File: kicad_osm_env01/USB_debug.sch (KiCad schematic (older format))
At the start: 22 parts, among them Q2 S8050, Q3 S8050, U13 CP2102N-A01-GQFN24

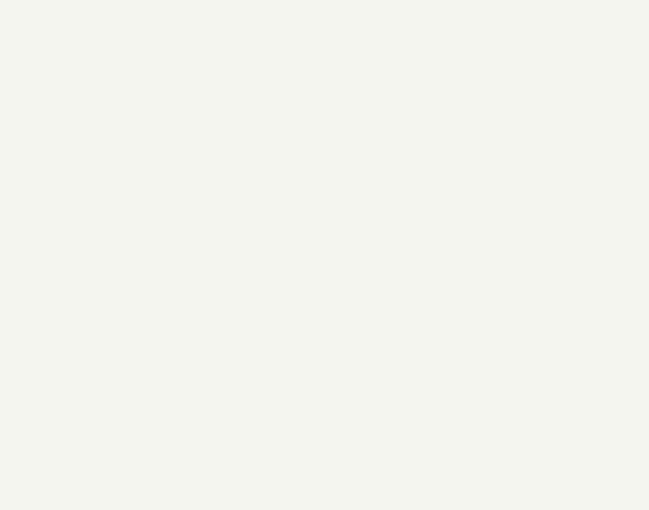
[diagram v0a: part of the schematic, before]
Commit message: pushed latest schematics got started with micro into schematic
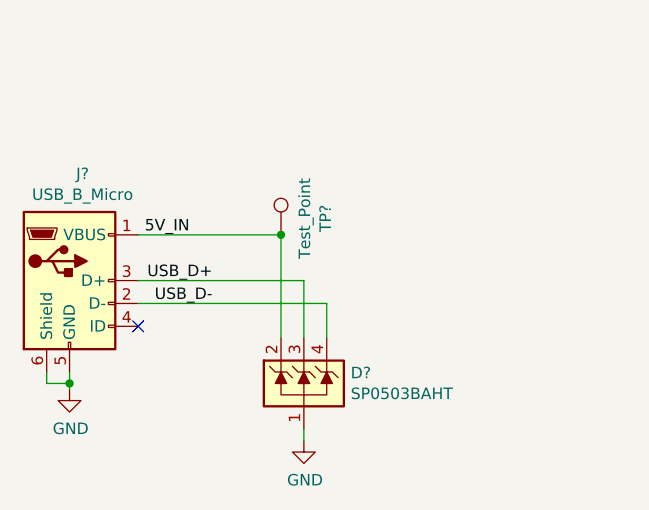
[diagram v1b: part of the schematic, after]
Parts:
- added D?: SP0503BAHT, Package_TO_SOT_SMD:SOT-143, symbol OSM_env01-rescue:SP0503BAHT-ESD_Protection-ESP32-EVB_Rev_D-rescue
- added J?: USB_B_Micro, Devtank_PCB_lib:MOLEX_105017-0001_USB_B, symbol Connector:USB_B_Micro
- added TP?: Test_Point, TestPoint:TestPoint_THTPad_D1.0mm_Drill0.5mm, symbol OSM_env01-rescue:Test_Point-Connector-ESP32-EVB_Rev_D-rescue
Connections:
- net GND: now also D?.1 (A), J?.5 (GND), J?.6 (Shield)
- new net 5V_IN: D?.2 (K), J?.1 (VBUS), TP?.1
- new net USB_D+: D?.3 (K), J?.3 (D+)
- new net USB_D-: D?.4 (K), J?.2 (D-)
- no-connect marks 5 -> 6
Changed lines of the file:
@@
 $Descr A4 11693 8268
 encoding utf-8
-Sheet 2 4
+Sheet 2 8
 Title "Open Smart Monitor"
 Date ""
@@
 Text Label 7825 4075 2    50   ~ 0
 ESP_RES2
+$Comp
+L Connector:USB_B_Micro J?
+U 1 1 6097E54E
+P 1900 5925
+AR Path="/6097E54E" Ref="J?"  Part="1"
+AR Path="/5F4610BE/6097E54E" Ref="J?"  Part="1"
+F 0 "J?" H 1957 6392 50  0000 C CNN
+F 1 "USB_B_Micro" H 1957 6301 50  0000 C CNN
+F 2 "Devtank_PCB_lib:MOLEX_105017-0001_USB_B" H 2050 5875 50  0001 C CNN
+F 3 "~" H 2050 5875 50  0001 C CNN
+	1    1900 5925
+	1    0    0    -1
+$EndComp
+Text Label 2425 5725 2    50   ~ 0
+5V_IN
+Text Label 2525 5925 2    50   ~ 0
+USB_D+
+Text Label 2525 6025 2    50   ~ 0
+USB_D-
+NoConn ~ 2200 6125
+$Comp
+L OSM_env01-rescue:SP0503BAHT-ESD_Protection-ESP32-EVB_Rev_D-rescue D?
+U 1 1 6097E558
+P 2925 6375
+AR Path="/6097E558" Ref="D?"  Part="1"
+AR Path="/5F4610BE/6097E558" Ref="D?"  Part="1"
+F 0 "D?" H 3130 6421 50  0000 L CNN
+F 1 "SP0503BAHT" H 3130 6330 50  0000 L CNN
+F 2 "Package_TO_SOT_SMD:SOT-143" H 3150 6325 50  0001 L CNN
+F 3 "http://www.littelfuse.com/~/media/files/littelfuse/technical%20resources/documents/data%20sheets/sp05xxba.pdf" H 3050 6500 50  0001 C CNN
+	1    2925 6375
+	1    0    0    -1
+$EndComp
+Wire Wire Line
+	2825 5725 2825 6175
+Wire Wire Line
+	2925 6175 2925 5925
+Wire Wire Line
+	2200 5925 2925 5925
+Wire Wire Line
+	3025 6175 3025 6025
+Wire Wire Line
+	2200 6025 3025 6025
+Wire Wire Line
+	2925 6575 2925 6625
+$Comp
+L OSM_env01-rescue:GND-ESP32-EVB_Rev_D #PWR?
+U 1 1 6097E564
+P 2925 6625
+AR Path="/6097E564" Ref="#PWR?"  Part="1"
+AR Path="/5F4610BE/6097E564" Ref="#PWR?"  Part="1"
+F 0 "#PWR?" H 2925 6375 50  0001 C CNN
+F 1 "GND" H 2930 6452 50  0000 C CNN
+F 2 "" H 2925 6625 60  0000 C CNN
+F 3 "" H 2925 6625 60  0000 C CNN
+	1    2925 6625
+	1    0    0    -1
+$EndComp
+$Comp
+L OSM_env01-rescue:GND-ESP32-EVB_Rev_D #PWR?
+U 1 1 6097E56A
+P 1900 6400
+AR Path="/6097E56A" Ref="#PWR?"  Part="1"
+AR Path="/5F4610BE/6097E56A" Ref="#PWR?"  Part="1"
+F 0 "#PWR?" H 1900 6150 50  0001 C CNN
+F 1 "GND" H 1905 6227 50  0000 C CNN
+F 2 "" H 1900 6400 60  0000 C CNN
+F 3 "" H 1900 6400 60  0000 C CNN
+	1    1900 6400
+	1    0    0    -1
+$EndComp
+$Comp
+L OSM_env01-rescue:Test_Point-Connector-ESP32-EVB_Rev_D-rescue TP?
+U 1 1 6097E570
+P 2825 5725
+AR Path="/6097E570" Ref="TP?"  Part="1"
+AR Path="/5F4610BE/6097E570" Ref="TP?"  Part="1"
+F 0 "TP?" V 3020 5797 50  0000 C CNN
+F 1 "Test_Point" V 2929 5797 50  0000 C CNN
+F 2 "TestPoint:TestPoint_THTPad_D1.0mm_Drill0.5mm" H 3025 5725 50  0001 C CNN
+F 3 "~" H 3025 5725 50  0001 C CNN
+	1    2825 5725
+	1    0    0    -1
+$EndComp
+Wire Wire Line
+	1900 6325 1900 6375
+Wire Wire Line
+	1800 6325 1800 6375
+Wire Wire Line
+	1800 6375 1900 6375
+Connection ~ 1900 6375
+Wire Wire Line
+	1900 6375 1900 6400
+Wire Wire Line
+	2200 5725 2825 5725
+Connection ~ 2825 5725
 $EndSCHEMATC

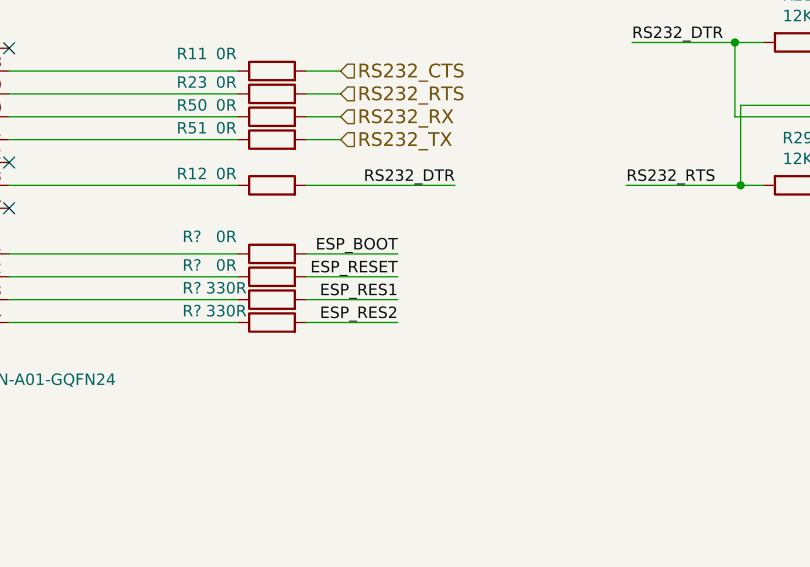
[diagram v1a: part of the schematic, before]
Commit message: stm32 added to kicad
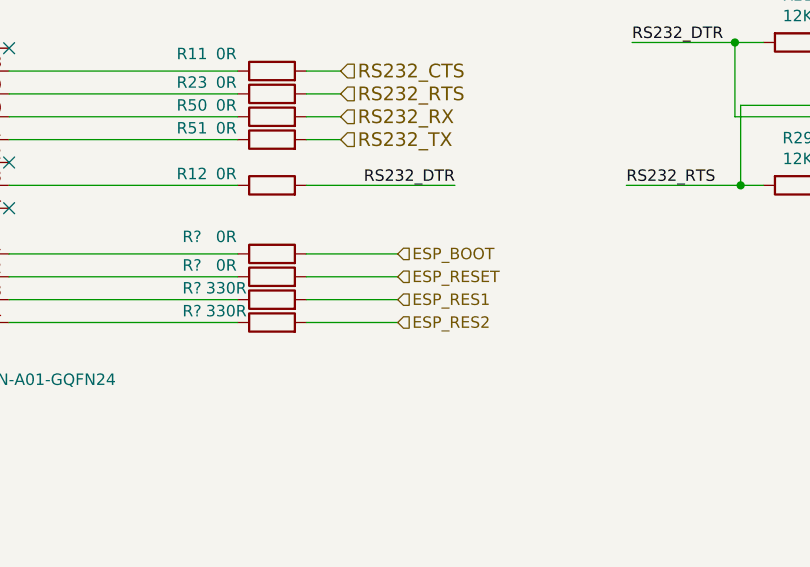
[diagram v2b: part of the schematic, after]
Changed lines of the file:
@@
 $Descr A4 11693 8268
 encoding utf-8
-Sheet 2 8
+Sheet 9 9
 Title "Open Smart Monitor"
 Date ""
@@
 Wire Wire Line
 	7425 4075 7825 4075
-Text Label 7825 3775 2    50   ~ 0
-ESP_BOOT
-Text Label 7825 3875 2    50   ~ 0
-ESP_RESET
 Wire Wire Line
 	7425 3775 7825 3775
 Wire Wire Line
 	7425 3875 7825 3875
-Text Label 7825 3975 2    50   ~ 0
-ESP_RES1
-Text Label 7825 4075 2    50   ~ 0
-ESP_RES2
 $Comp
 L Connector:USB_B_Micro J?
@@
 	2200 5725 2825 5725
 Connection ~ 2825 5725
+Text HLabel 7825 3775 2    50   Input ~ 0
+ESP_BOOT
+Text HLabel 7825 3875 2    50   Input ~ 0
+ESP_RESET
+Text HLabel 7825 3975 2    50   Input ~ 0
+ESP_RES1
+Text HLabel 7825 4075 2    50   Input ~ 0
+ESP_RES2
 $EndSCHEMATC

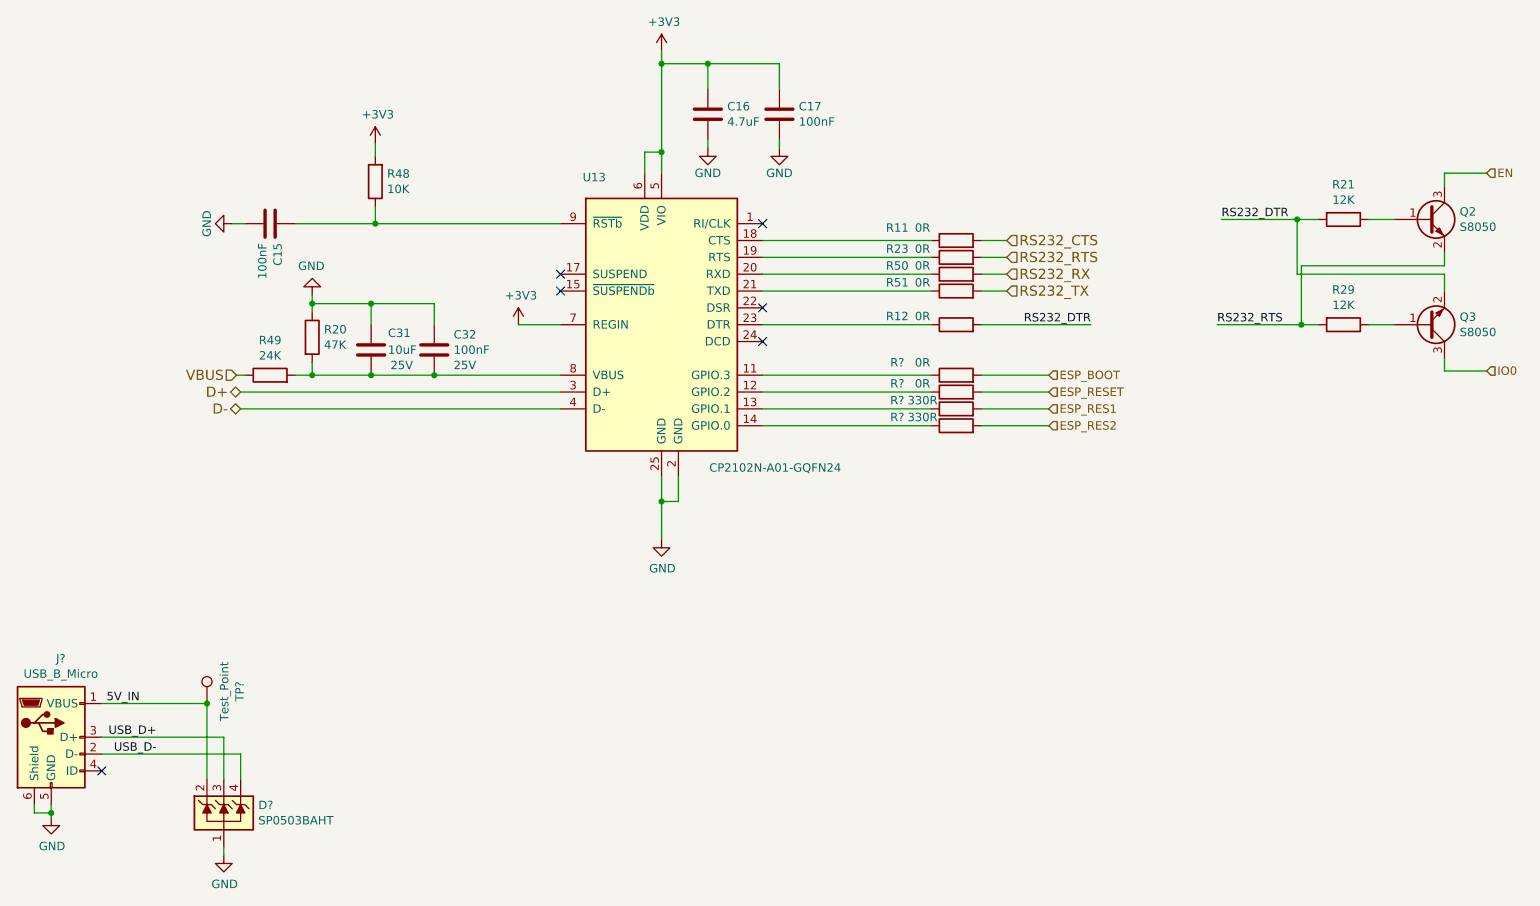
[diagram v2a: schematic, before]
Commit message: updated schematics
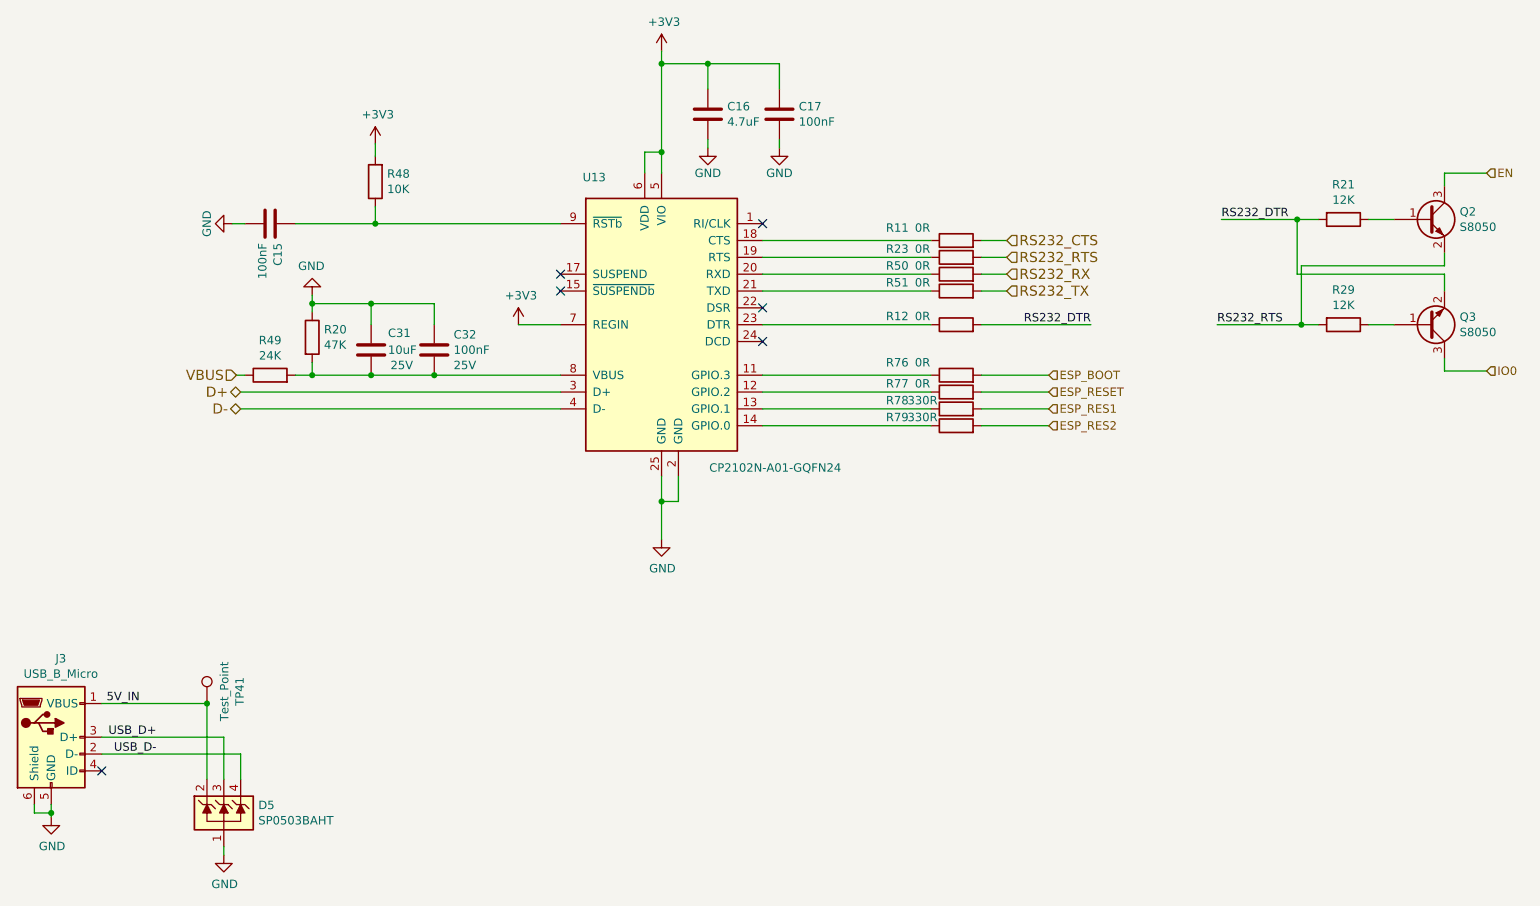
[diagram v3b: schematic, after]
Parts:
- gave numbers to parts that had none: 7
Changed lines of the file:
@@
 $Descr A4 11693 8268
 encoding utf-8
-Sheet 9 9
+Sheet 9 11
 Title "Open Smart Monitor"
 Date ""
@@
 	6125 4075 7125 4075
 $Comp
-L OSM_env01-rescue:R-device-ESP32-EVB_Rev_D-rescue R?
+L OSM_env01-rescue:R-device-ESP32-EVB_Rev_D-rescue R78
 U 1 1 5F5D6C15
 P 7275 3975
-F 0 "R?" V 7325 4325 50  0000 C CNN
+F 0 "R78" V 7325 4325 50  0000 C CNN
 F 1 "330R" V 7325 4175 50  0000 C CNN
 F 2 "Resistor_SMD:R_0603_1608Metric" V 7205 3975 50  0001 C CNN
@@
 $EndComp
 $Comp
-L OSM_env01-rescue:R-device-ESP32-EVB_Rev_D-rescue R?
+L OSM_env01-rescue:R-device-ESP32-EVB_Rev_D-rescue R79
 U 1 1 5F5D6C1B
 P 7275 4075
-F 0 "R?" V 7325 4425 50  0000 C CNN
+F 0 "R79" V 7325 4425 50  0000 C CNN
 F 1 "330R" V 7325 4275 50  0000 C CNN
 F 2 "Resistor_SMD:R_0603_1608Metric" V 7205 4075 50  0001 C CNN
@@
 	6125 3875 7125 3875
 $Comp
-L OSM_env01-rescue:R-device-ESP32-EVB_Rev_D-rescue R?
+L OSM_env01-rescue:R-device-ESP32-EVB_Rev_D-rescue R76
 U 1 1 5F5D6C24
 P 7275 3775
-F 0 "R?" V 7350 4125 50  0000 C CNN
+F 0 "R76" V 7350 4125 50  0000 C CNN
 F 1 "0R" V 7350 3975 50  0000 C CNN
 F 2 "Resistor_SMD:R_0603_1608Metric" V 7205 3775 50  0001 C CNN
@@
 $EndComp
 $Comp
-L OSM_env01-rescue:R-device-ESP32-EVB_Rev_D-rescue R?
+L OSM_env01-rescue:R-device-ESP32-EVB_Rev_D-rescue R77
 U 1 1 5F5D6C2A
 P 7275 3875
-F 0 "R?" V 7325 4225 50  0000 C CNN
+F 0 "R77" V 7325 4225 50  0000 C CNN
 F 1 "0R" V 7325 4075 50  0000 C CNN
 F 2 "Resistor_SMD:R_0603_1608Metric" V 7205 3875 50  0001 C CNN
@@
 P 1900 5925
 AR Path="/6097E54E" Ref="J?"  Part="1"
-AR Path="/5F4610BE/6097E54E" Ref="J?"  Part="1"
-F 0 "J?" H 1957 6392 50  0000 C CNN
+AR Path="/5F4610BE/6097E54E" Ref="J3"  Part="1"
+F 0 "J3" H 1957 6392 50  0000 C CNN
 F 1 "USB_B_Micro" H 1957 6301 50  0000 C CNN
 F 2 "Devtank_PCB_lib:MOLEX_105017-0001_USB_B" H 2050 5875 50  0001 C CNN
@@
 P 2925 6375
 AR Path="/6097E558" Ref="D?"  Part="1"
-AR Path="/5F4610BE/6097E558" Ref="D?"  Part="1"
-F 0 "D?" H 3130 6421 50  0000 L CNN
+AR Path="/5F4610BE/6097E558" Ref="D5"  Part="1"
+F 0 "D5" H 3130 6421 50  0000 L CNN
 F 1 "SP0503BAHT" H 3130 6330 50  0000 L CNN
 F 2 "Package_TO_SOT_SMD:SOT-143" H 3150 6325 50  0001 L CNN
@@
 P 2925 6625
 AR Path="/6097E564" Ref="#PWR?"  Part="1"
-AR Path="/5F4610BE/6097E564" Ref="#PWR?"  Part="1"
-F 0 "#PWR?" H 2925 6375 50  0001 C CNN
+AR Path="/5F4610BE/6097E564" Ref="#PWR059"  Part="1"
+F 0 "#PWR059" H 2925 6375 50  0001 C CNN
 F 1 "GND" H 2930 6452 50  0000 C CNN
 F 2 "" H 2925 6625 60  0000 C CNN
@@
 P 1900 6400
 AR Path="/6097E56A" Ref="#PWR?"  Part="1"
-AR Path="/5F4610BE/6097E56A" Ref="#PWR?"  Part="1"
-F 0 "#PWR?" H 1900 6150 50  0001 C CNN
+AR Path="/5F4610BE/6097E56A" Ref="#PWR058"  Part="1"
+F 0 "#PWR058" H 1900 6150 50  0001 C CNN
 F 1 "GND" H 1905 6227 50  0000 C CNN
 F 2 "" H 1900 6400 60  0000 C CNN
@@
 P 2825 5725
 AR Path="/6097E570" Ref="TP?"  Part="1"
-AR Path="/5F4610BE/6097E570" Ref="TP?"  Part="1"
-F 0 "TP?" V 3020 5797 50  0000 C CNN
+AR Path="/5F4610BE/6097E570" Ref="TP41"  Part="1"
+F 0 "TP41" V 3020 5797 50  0000 C CNN
 F 1 "Test_Point" V 2929 5797 50  0000 C CNN
 F 2 "TestPoint:TestPoint_THTPad_D1.0mm_Drill0.5mm" H 3025 5725 50  0001 C CNN

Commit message: schematics awaiting review
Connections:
- net D+ is gone; now on net USB_D+: U13.3 (D+)
- net D- is gone; now on net USB_D-: U13.4 (D-)
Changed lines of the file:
@@
 $Descr A4 11693 8268
 encoding utf-8
-Sheet 9 11
+Sheet 5 11
 Title "Open Smart Monitor"
 Date ""
@@
 Text HLabel 7575 3275 2    60   Input ~ 0
 RS232_TX
-Text HLabel 3025 3875 0    60   BiDi ~ 0
-D+
-Text HLabel 3025 3975 0    60   BiDi ~ 0
-D-
 $Comp
 L OSM_env01-rescue:CP2102N-A01-GQFN24-silabs-Sensi_Board-rescue-ESP32-EVB_Rev_D-rescue U13
@@
 Wire Wire Line
 	3050 2875 2975 2875
-Wire Wire Line
-	3025 3875 4925 3875
-Wire Wire Line
-	3025 3975 4925 3975
 $Comp
 L OSM_env01-rescue:R-device-ESP32-EVB_Rev_D-rescue R20
@@
 Text HLabel 7825 4075 2    50   Input ~ 0
 ESP_RES2
+Text Label 4550 3875 0    50   ~ 0
+USB_D+
+Text Label 4550 3975 0    50   ~ 0
+USB_D-
+Wire Wire Line
+	4925 3875 4550 3875
+Wire Wire Line
+	4925 3975 4550 3975
 $EndSCHEMATC

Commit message: started layout
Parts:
- J3: footprint Devtank_PCB_lib:MOLEX_105017-0001_USB_B -> Devtank_PCB_lib:MOLEX_105017-0001_Micro_USB_b
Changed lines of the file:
@@
 $Descr A4 11693 8268
 encoding utf-8
-Sheet 5 12
+Sheet 5 11
 Title "Open Smart Monitor"
 Date ""
@@
 F 0 "J3" H 1957 6392 50  0000 C CNN
 F 1 "USB_B_Micro" H 1957 6301 50  0000 C CNN
-F 2 "Devtank_PCB_lib:MOLEX_105017-0001_USB_B" H 2050 5875 50  0001 C CNN
+F 2 "Devtank_PCB_lib:MOLEX_105017-0001_Micro_USB_b" H 2050 5875 50  0001 C CNN
 F 3 "~" H 2050 5875 50  0001 C CNN
 	1    1900 5925

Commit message: Throwdown of parts
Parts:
- C15: footprint Capacitor_SMD:C_0603_1608Metric -> Capacitor_SMD:C_0402_1005Metric
- C31: footprint Capacitor_SMD:C_0603_1608Metric -> Capacitor_SMD:C_0805_2012Metric
- U13: footprint Devtank_PCB_lib:CP2102-24-QFN_pad0.3mm -> Devtank_PCB_lib:CP2102n_qfn-24_ep-2.6x2.6_thermalvias-0.3
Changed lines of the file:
@@
 F 0 "U13" H 5125 4350 50  0000 C CNN
 F 1 "CP2102N-A01-GQFN24" H 6200 2625 50  0000 C CNN
-F 2 "Devtank_PCB_lib:CP2102-24-QFN_pad0.3mm" H 5975 2675 50  0001 L CNN
+F 2 "Devtank_PCB_lib:CP2102n_qfn-24_ep-2.6x2.6_thermalvias-0.3" H 5975 2675 50  0001 L CNN
 F 3 "http://www.silabs.com/support%20documents/technicaldocs/cp2102n-datasheet.pdf" H 5575 2425 50  0001 C CNN
 F 4 "118-007" H 5525 3475 50  0001 C CNN "Devtank"
@@
 F 0 "C15" H 3315 2921 50  0000 L CNN
 F 1 "100nF" H 3315 2830 50  0000 L CNN
-F 2 "Capacitor_SMD:C_0603_1608Metric" H 3238 2725 50  0001 C CNN
+F 2 "Capacitor_SMD:C_0402_1005Metric" H 3238 2725 50  0001 C CNN
 F 3 "" H 3200 2875 50  0001 C CNN
 	1    3200 2875
@@
 F 0 "C31" H 3900 3725 50  0000 L CNN
 F 1 "10uF" H 3900 3625 50  0000 L CNN
-F 2 "Capacitor_SMD:C_0603_1608Metric" H 3838 3475 50  0001 C CNN
+F 2 "Capacitor_SMD:C_0805_2012Metric" H 3838 3475 50  0001 C CNN
 F 3 "" H 3800 3625 50  0001 C CNN
 F 4 "25V" H 3915 3534 50  0000 L CNN "Voltage"

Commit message: updated 3d step file
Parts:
- added J7: 632723100011, Devtank_PCB_lib:WURTH_632723100011_USB_C, symbol Devtank:632723100011
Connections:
- new net: J7.A1 (GNDA), J7.A12 (GNDA)
- new net: J7.A4 (VBUS_A), J7.A9 (VBUS_A)
- new net: J7.B1 (GNDB), J7.B12 (GNDB)
- new net: J7.B4 (VBUS_B), J7.B9 (VBUS_B)
- new net: J7.G1 (GND), J7.G2 (GND)
- new net: J7.S1 (SHIELD), J7.S2 (SHIELD), J7.S3 (SHIELD), J7.S4 (SHIELD), J7.S5 (SHIELD), J7.S6 (SHIELD)
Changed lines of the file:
@@
 Wire Wire Line
 	4925 3975 4550 3975
+$Comp
+L Devtank:632723100011 J7
+U 1 1 6128CA6C
+P 4975 5975
+F 0 "J7" H 4975 6742 50  0000 C CNN
+F 1 "632723100011" H 4975 6651 50  0000 C CNN
+F 2 "Devtank_PCB_lib:WURTH_632723100011_USB_C" H 4975 5975 50  0001 L BNN
+F 3 "" H 4975 5975 50  0001 L BNN
+F 4 "3.41 mm" H 4975 5975 50  0001 L BNN "MAXIMUM_PACKAGE_HEIGHT"
+F 5 "Wurth Electronics" H 4975 5975 50  0001 L BNN "MANUFACTURER"
+F 6 "001.003" H 4975 5975 50  0001 L BNN "PARTREV"
+F 7 "Manufacturer Recommendations" H 4975 5975 50  0001 L BNN "STANDARD"
+	1    4975 5975
+	1    0    0    -1
+$EndComp
 $EndSCHEMATC
